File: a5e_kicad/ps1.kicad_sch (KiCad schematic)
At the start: 80 parts, among them U16 AP61202Z6, U18 AP61202Z6, U19 AP61202Z6, U8 AP61202Z6

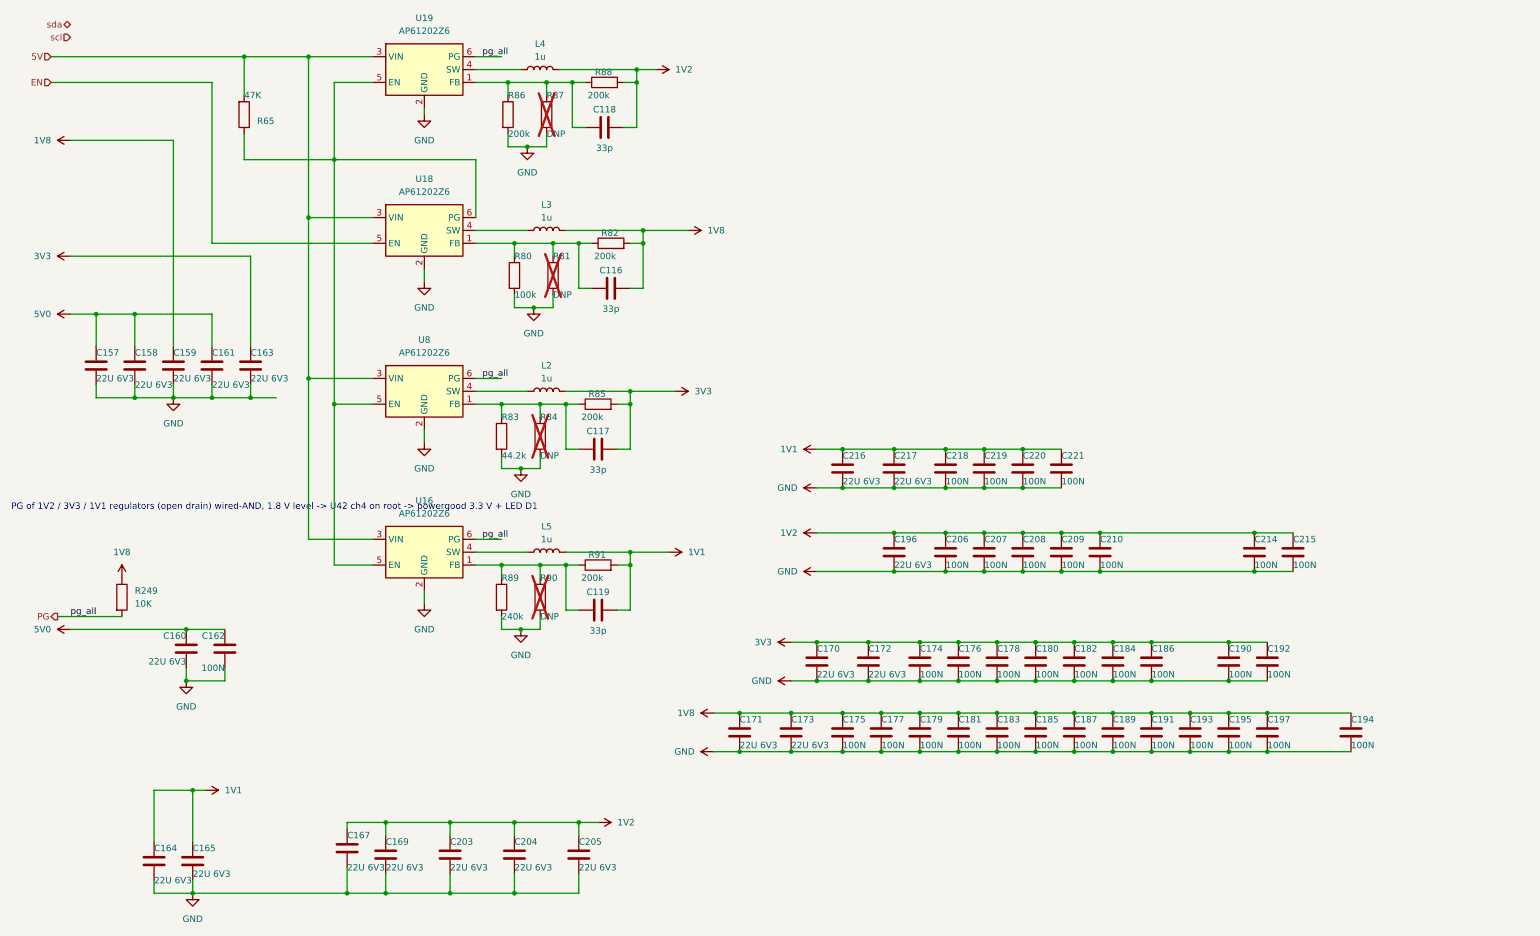
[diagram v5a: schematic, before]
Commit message: Schematic reorg step 2: per-rail power symbols, real GND symbols, PWR_FLAGs, U12 in project library
Netlist: 0 renamed, 0 connectivity diffs; DRC parity 0. ERC 234 -> 224 (with the KiCad symbol libraries).
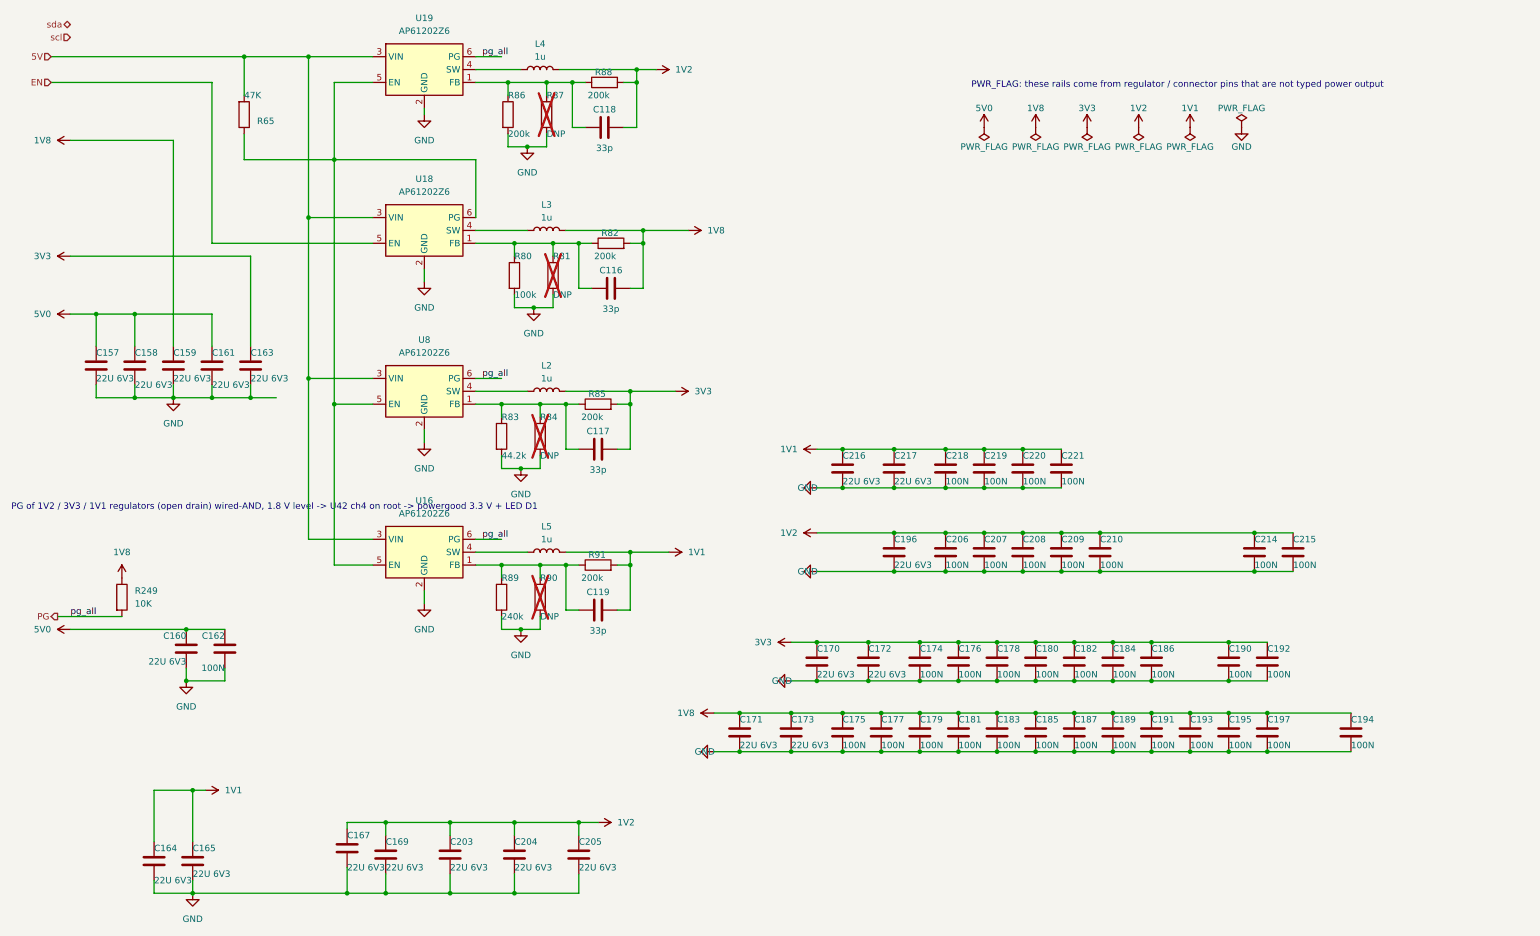
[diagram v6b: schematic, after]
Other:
- note added: "PWR_FLAG: these rails come from regulator / connector pins that are not typed power output"

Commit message: Schematic reorg step 3: U42 cluster on grid, U2 symbol redrawn, notes wrapped inside the frame
Netlist: 0 renamed, 0 connectivity diffs; DRC parity 0. ERC 223 -> 199 (no off-grid endpoints).
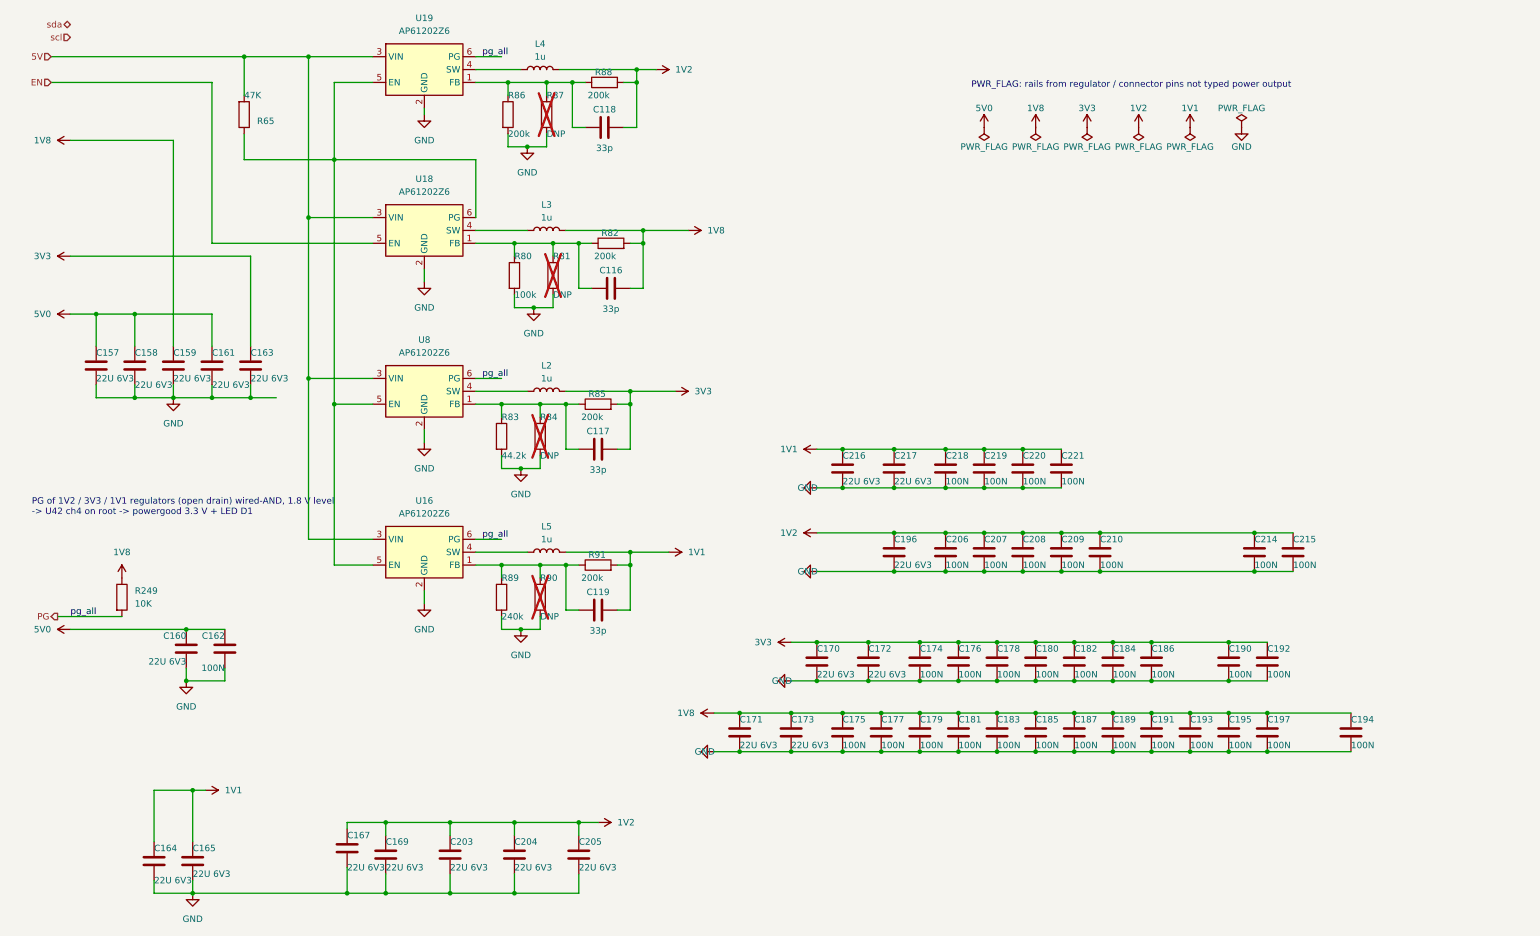
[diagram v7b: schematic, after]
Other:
- note added: "PWR_FLAG: rails from regulator / connector pins not typed power output"
- note removed: "PWR_FLAG: these rails come from regulator / connector pins that are not typed power output"
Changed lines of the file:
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@@
 		(comment 1 "${BOARD}")
 	)
-	(text "PG of 1V2 / 3V3 / 1V1 regulators (open drain) wired-AND, 1.8 V level -> U42 ch4 on root -> powergood 3.3 V + LED D1"
+	(text "PG of 1V2 / 3V3 / 1V1 regulators (open drain) wired-AND, 1.8 V level\n-> U42 ch4 on root -> powergood 3.3 V + LED D1"
 		(exclude_from_sim no)
-		(at 11.176 113.03 0)
+		(at 15.24 113.03 0)
 		(effects
 			(font
@@
 		)
 	)
-	(text "PWR_FLAG: these rails come from regulator / connector pins that are not typed power output"
+	(text "PWR_FLAG: rails from regulator / connector pins not typed power output"
 		(exclude_from_sim no)
 		(at 200.66 30.48 0)

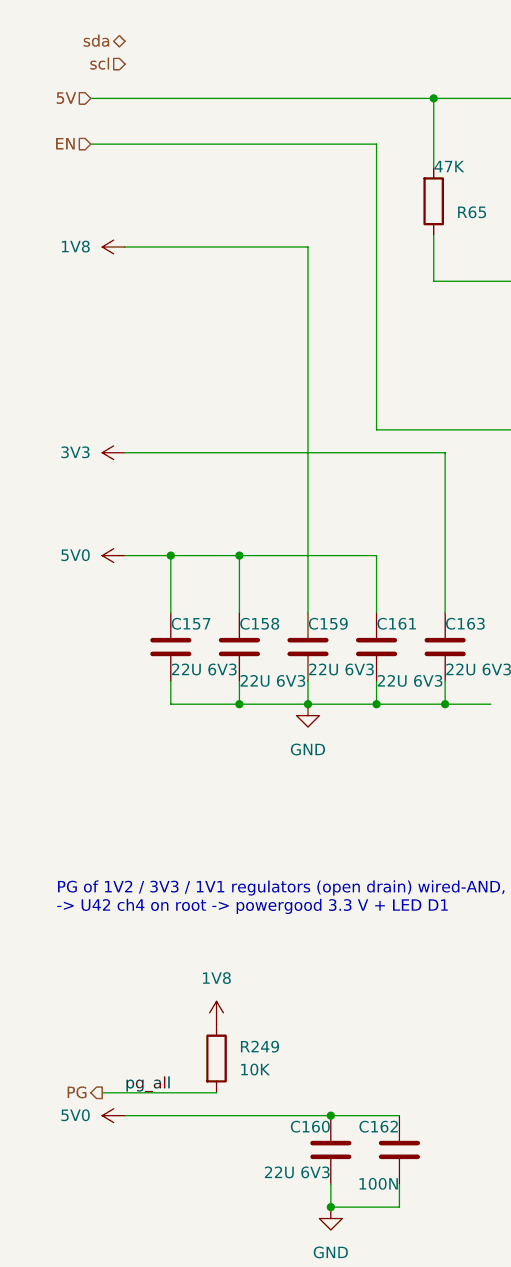
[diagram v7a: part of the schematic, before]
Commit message: Schematic reorg step 4: one name per net
- SoC power: drop the 13 vcc* labels; U7 VCCADC/VCCPLL1_HPS (1V8) and
  VCCPLLDIG_SDM/VCCPLLDIG1_HPS (VCORE) get rail symbols instead
- 5V hierarchical labels and sheet pins renamed to 5V0
- HPS cold reset is a local net in SDM (hps_cold_rst_n); unused sheet pin removed
- Power-good chain: pg_vcore, pg_all (local), pg_all_3v3 (was pg_led)
- sdm_clk25 global labels made local
- JTAG labels jtag_{tdi,tck,tms,tdo}_3v3 on the U1-J1 nets
- PCB net names updated to match (9 renames, no connectivity change)

ERC 199 -> 183. DRC unchanged (295 / 174 unconnected / parity 0).
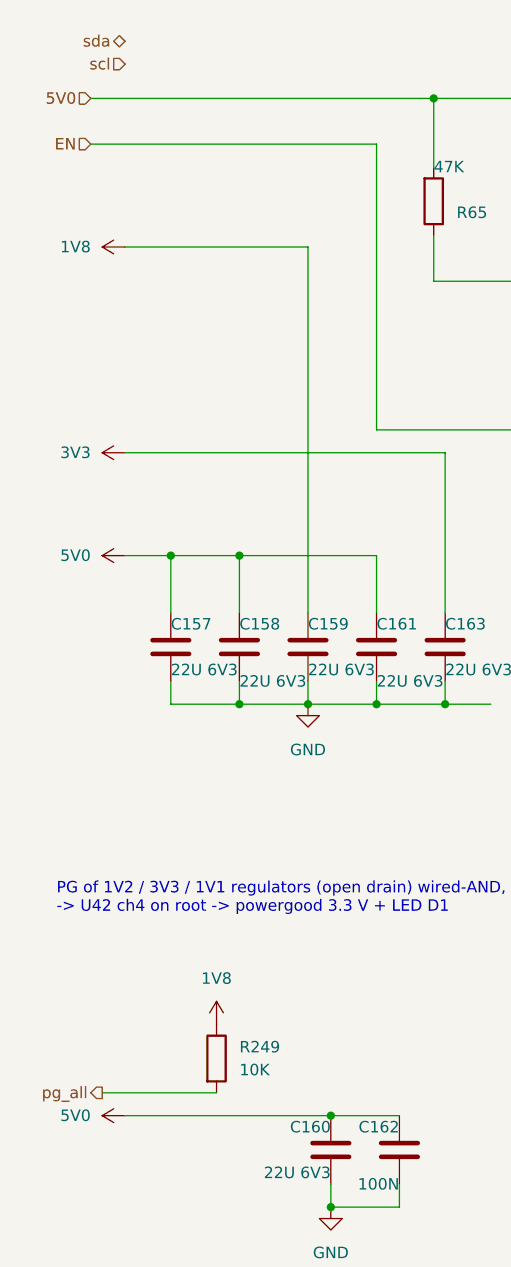
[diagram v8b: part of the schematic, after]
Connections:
- net 5V is gone; now on net 5V0: R65.2, U16.3 (VIN), U18.3 (VIN), U19.3 (VIN), U8.3 (VIN)
- net PG renamed pg_all
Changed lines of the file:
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@@
-	)
-	(label "pg_all"
-		(at 22.86 134.62 0)
-		(effects
-			(font
-				(size 1.27 1.27)
-			)
-			(justify left bottom)
-		)
 	)
 	(label "pg_all"
@@
 		)
 	)
-	(hierarchical_label "PG"
+	(hierarchical_label "pg_all"
 		(shape output)
 		(at 20.32 134.62 180)
@@
 		)
 	)
-	(hierarchical_label "5V"
+	(hierarchical_label "5V0"
 		(shape input)
 		(at 19.05 24.13 180)
